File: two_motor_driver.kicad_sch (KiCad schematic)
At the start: 33 parts, among them J1 Conn_01x02, J2 ESP PROG, J3 Conn_01x08, J5 Conn_01x01, J6 Conn_01x01, J7 Conn_01x01, M1 Conn_01x02, M2 Conn_01x02, SW1 SW_SPDT, SW2 SW_Push, U1 Teensy4.0, U2 ESP32-C3-DevKitM-1, U5 my_buck_boost

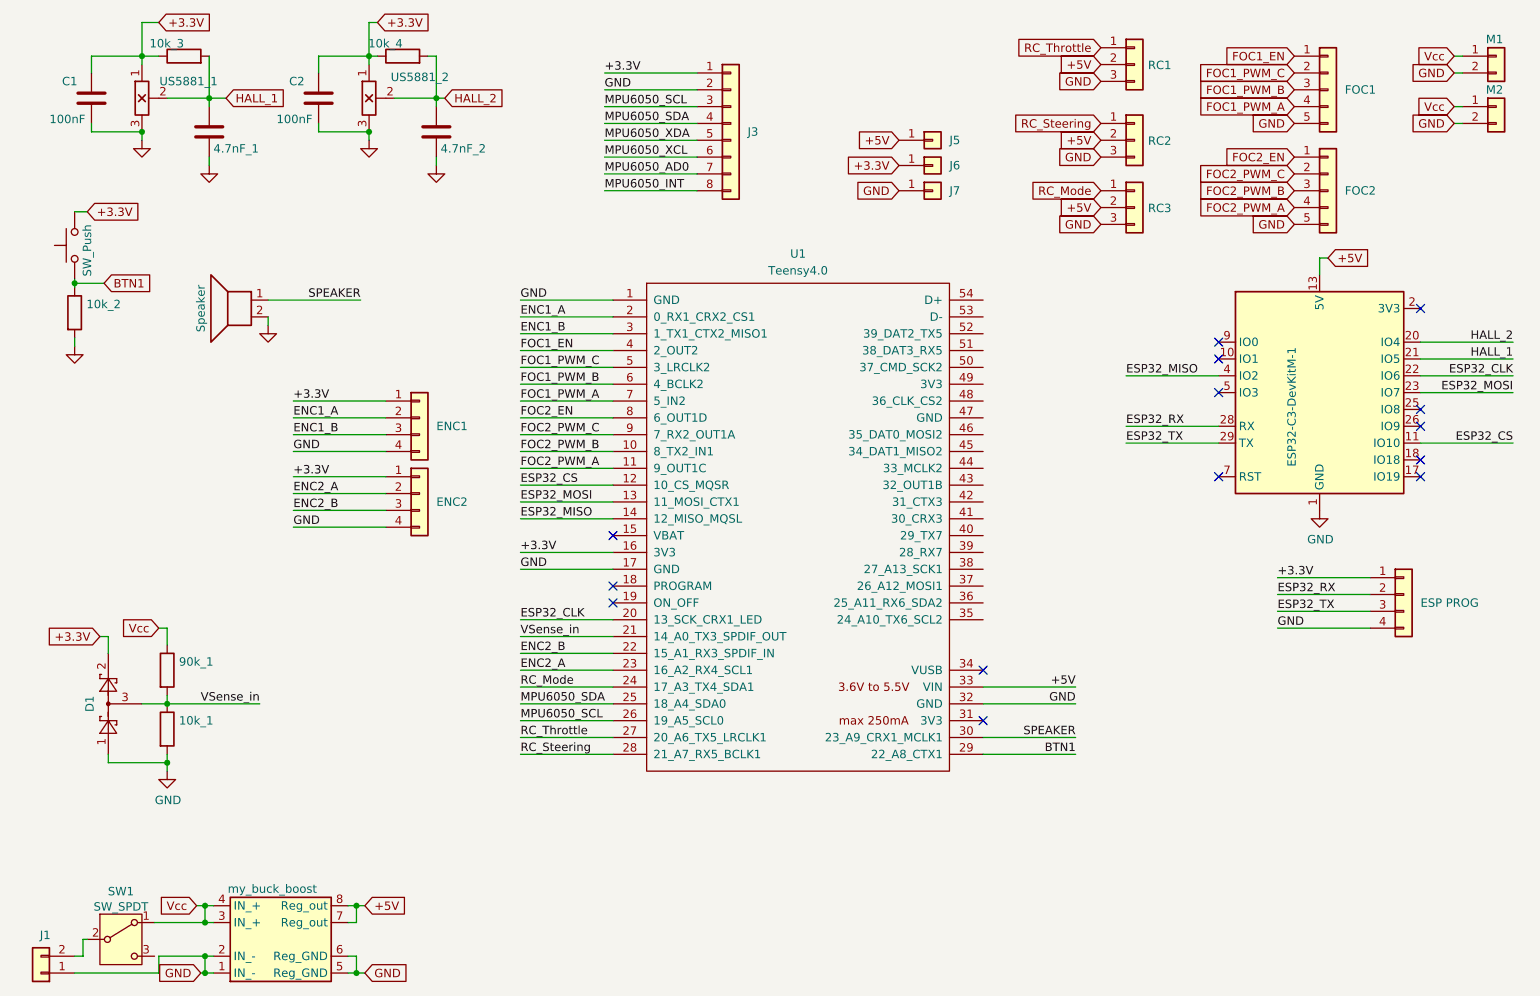
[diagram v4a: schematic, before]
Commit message: added DRV8313
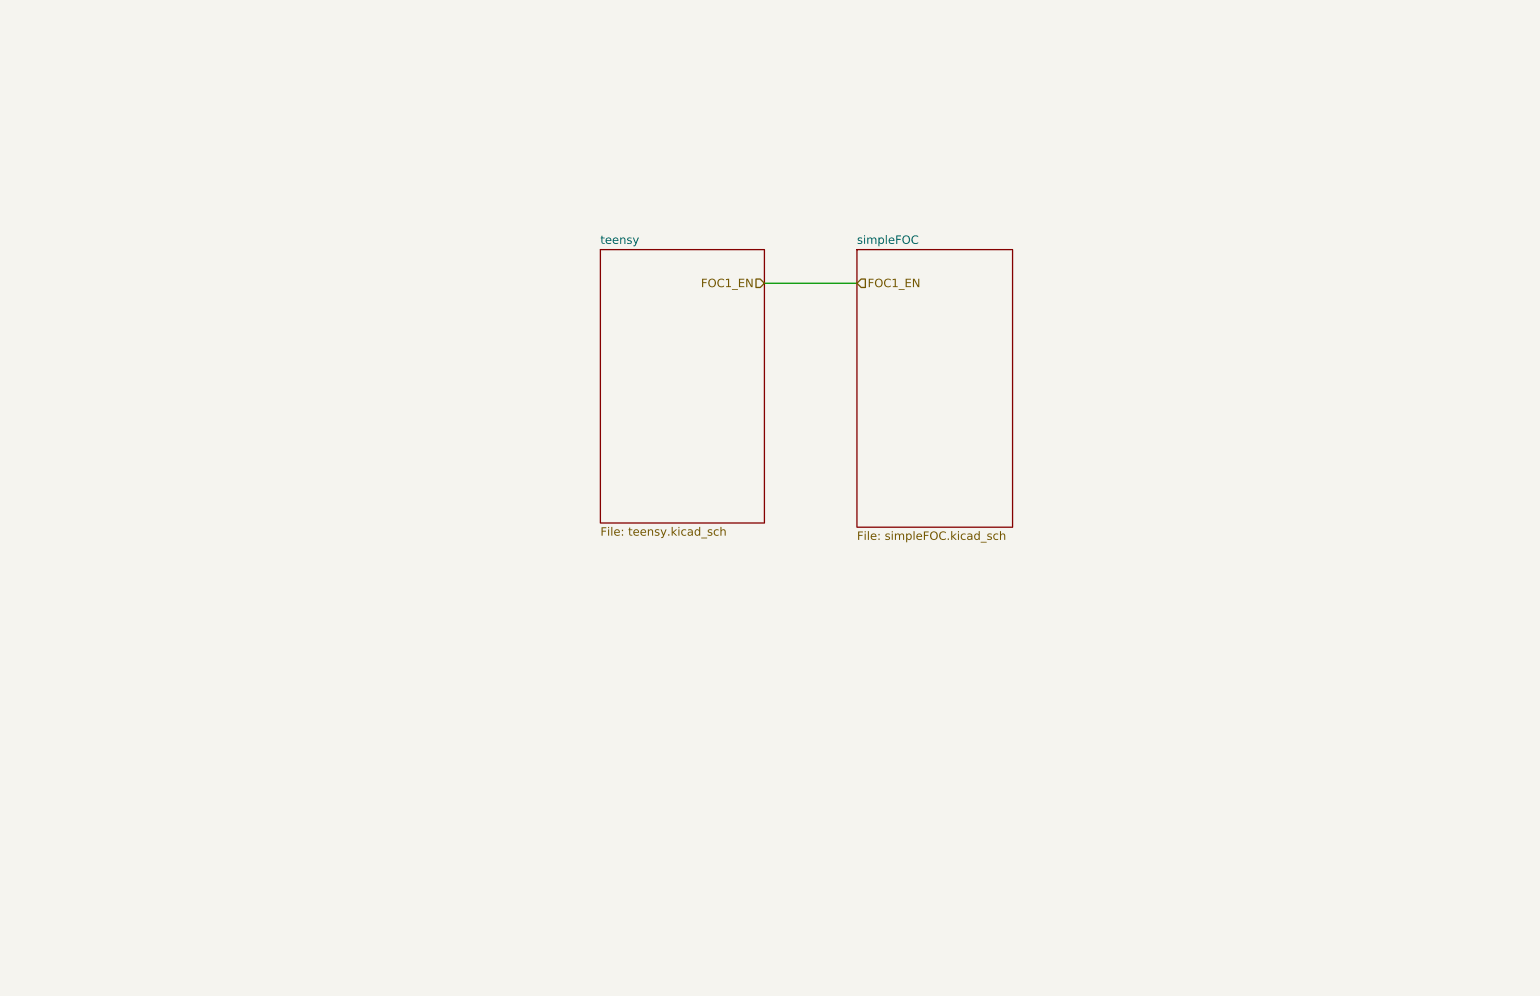
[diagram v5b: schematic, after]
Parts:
- removed 10k_1, 10k_2, 10k_3, 10k_4: 10k, Resistor_SMD:R_0805_2012Metric, symbol Device:R
- removed 4.7nF_1, 4.7nF_2: 4.7nF, Capacitor_SMD:C_0805_2012Metric, symbol Device:C
- removed 90k_1: 90k, Resistor_SMD:R_0805_2012Metric, symbol Device:R
- removed C1, C2: 100nF, Capacitor_SMD:C_0805_2012Metric, symbol Device:C
- removed D1: BAT54S, Package_TO_SOT_SMD:SOT-23-3, symbol two_motor_driver-rescue:BAT54S-Diode
- removed ENC1, ENC2: J1, Connector_PinSocket_2.54mm:PinSocket_1x04_P2.54mm_Vertical, symbol Connector_Generic:Conn_01x04
- removed FOC1, FOC2: Conn_01x05, Connector_PinSocket_2.54mm:PinSocket_1x05_P2.54mm_Vertical, symbol Connector_Generic:Conn_01x05
- removed J1, M1, M2: Conn_01x02, Connector_PinHeader_2.54mm:PinHeader_1x02_P2.54mm_Vertical, symbol Connector_Generic:Conn_01x02
- removed J2: ESP PROG, Connector_PinSocket_2.54mm:PinSocket_1x04_P2.54mm_Vertical, symbol Connector_Generic:Conn_01x04
- removed J3: Conn_01x08, Connector_PinSocket_2.54mm:PinSocket_1x08_P2.54mm_Vertical, symbol Connector_Generic:Conn_01x08
- removed J5, J6, J7: Conn_01x01, Connector_PinSocket_2.54mm:PinSocket_1x01_P2.54mm_Vertical, symbol Connector_Generic:Conn_01x01
- removed LS1: Speaker, CDS-13138-SMT-TR:SPKR_CDS-13138-SMT-TR, symbol Device:Speaker
- removed RC1, RC2, RC3: Conn_01x03, Connector_PinHeader_2.54mm:PinHeader_1x03_P2.54mm_Vertical, symbol Connector_Generic:Conn_01x03
- removed SW1: SW_SPDT, Button_Switch_THT:SW_NKK_BB15AH, symbol Switch:SW_SPDT
- removed SW2: SW_Push, Button_Switch_SMD:SW_Push_SPST_NO_Alps_SKRK, symbol Switch:SW_Push
- removed U1: Teensy4.0, simpleFOC_board:Teensy40, symbol teensy:Teensy4.0
- removed U2: ESP32-C3-DevKitM-1, RF_Module:ESP32-C3-DevKitM-1, symbol RF_Module:ESP32-C3-DevKitM-1
- removed U5: my_buck_boost, Converter_DCDC:my_buck_boost, symbol two_motor_driver-rescue:my_buck_boost-Regulator_Switching
- removed US5881_1, US5881_2: hall_effect_three_wire, Connector_PinHeader_2.54mm:PinHeader_1x03_P2.54mm_Vertical, symbol two_motor_driver-rescue:hall_effect_three_wire-Device
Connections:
- no-connect marks 14 -> 0
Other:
- added sheet simpleFOC (simpleFOC.kicad_sch)
- added sheet teensy (teensy.kicad_sch)

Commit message: jlcpcb order Y34-4852697
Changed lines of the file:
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@@
 	(generator_version "8.0")
 	(paper "User" 254 177.8)
-	(wire
-		(pts
-			(xy 125.73 57.15) (xy 139.7 57.15)
-		)
-		(stroke
-			(width 0)
-			(type default)
-		)
-	)
-	(hierarchical_label "FOC1_EN"
-		(shape input)
-		(at 125.73 57.15 180)
-		(effects
-			(font
-				(size 1.27 1.27)
-			)
-			(justify right)
-		)
-	)
-	(hierarchical_label "FOC1_EN"
-		(shape input)
-		(at 139.7 57.15 0)
-		(effects
-			(font
-				(size 1.27 1.27)
-			)
-			(justify left)
-		)
-	)
 	(sheet
 		(at 100.965 52.07)
